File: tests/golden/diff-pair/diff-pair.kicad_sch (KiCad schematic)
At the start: 7 parts, among them J1 USB_MICRO_B, J2 CONN_BRK_1X04

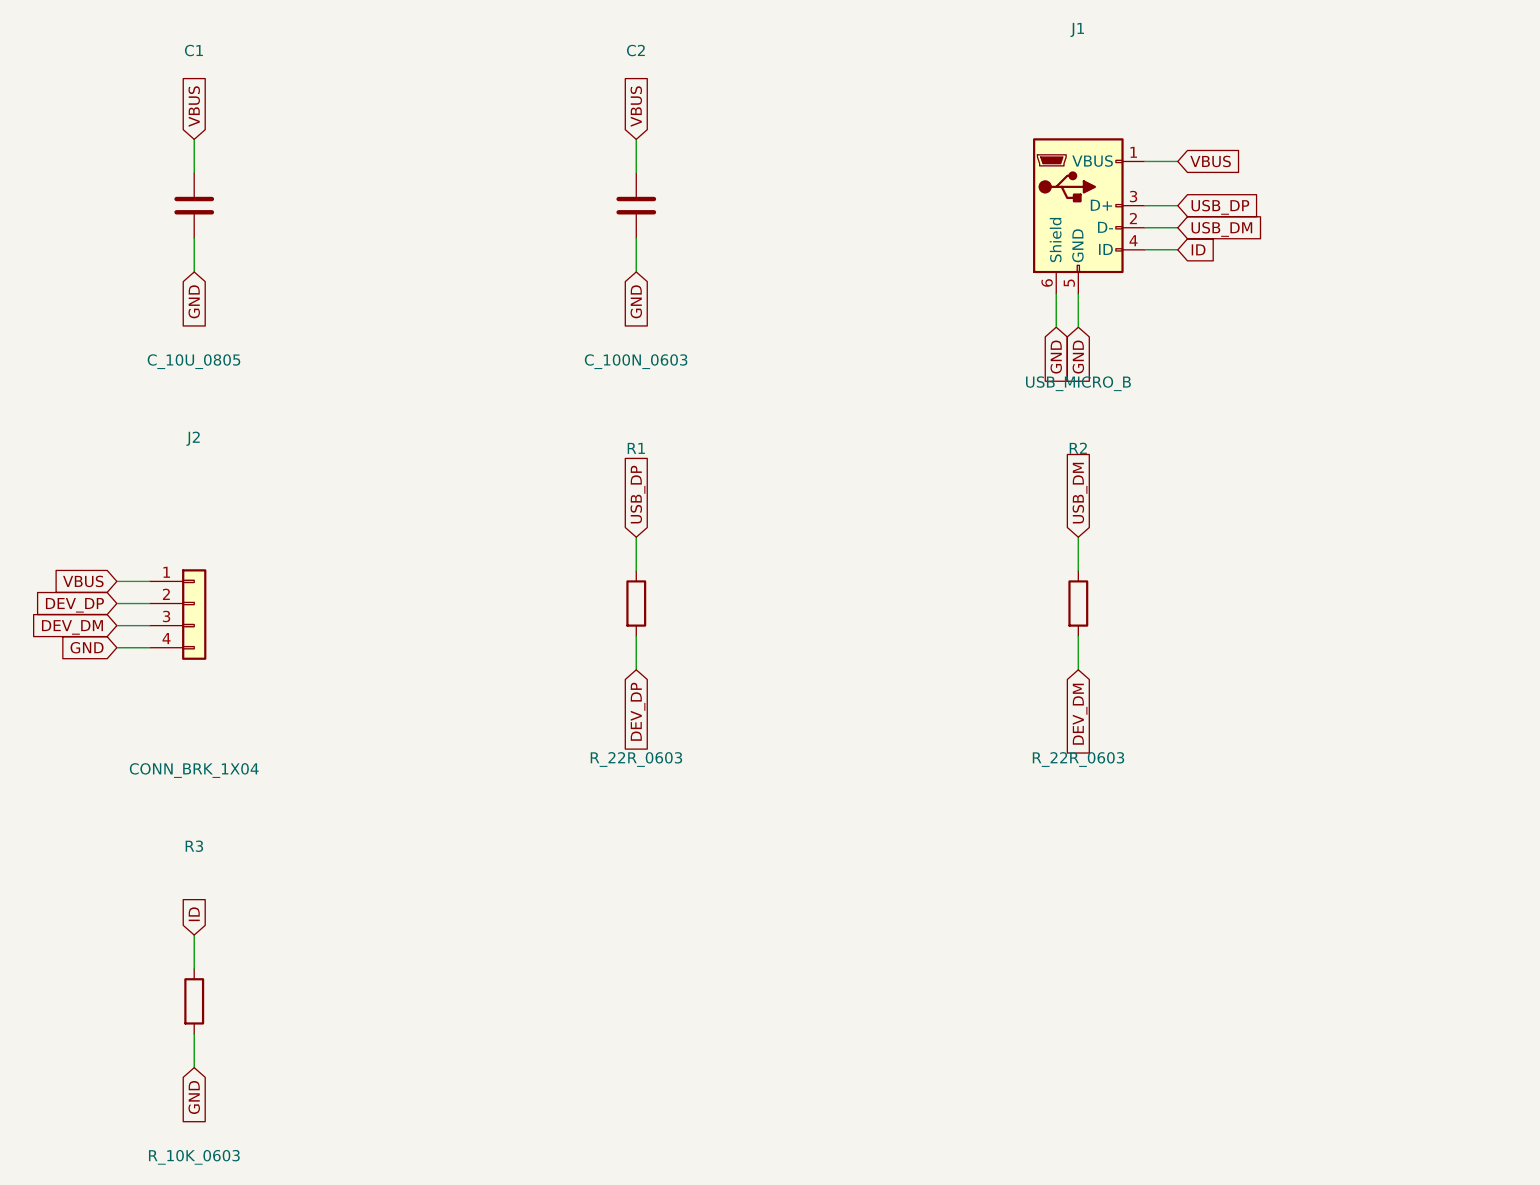
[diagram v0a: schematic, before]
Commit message: M7d: differential pairs routed as pairs, with honest limits
A pair's impedance comes from the coupling between its halves, so routing them
independently routes something else with the same netlist. A pair is now tightened
once, as a single centre-line wide enough for both traces and the gap, then offset
to either side. The gap is correct everywhere by construction, corners included,
and the halves come out the same length: 43.00 mm each with 0.000 mm skew on the
new diff-pair example.

Where a class gives an impedance but no gap, the gap is estimated from the standard
edge-coupled microstrip formula and reported as an estimate. Where the target is
unreachable by spacing at all — a 0.34 mm trace on 0.7 mm of dielectric spans only
about 102-195 ohm however far apart the halves go — that is said plainly rather
than clamped, because the fix is the trace width or the stackup and clamping would
hide it.

Coupled routing checks its own output and falls back rather than shipping something
that only looks like a pair. It refuses an ambiguous pair, one that would need a
crossover, one that would be mostly fan-out, and one whose fan-out would not clear
an obstacle it then names. Both of usb-port's pairs refuse, each saying which.

That self-checking is the reason DRC stays clean: the tightener guarantees
clearance for the centre-line, but the fan-out at each end is constructed rather
than tightened, and an early version of it landed 27 violations including shorts.
Checking beats hoping.

All five examples now route with zero DRC violations and zero schematic-parity
issues. Also implements `region_mm` placement rules, which the model promised and
the placer had been ignoring.

Not built, and said so in the docs rather than left to be discovered: meander
insertion for length matching, and pair crossovers. Skew is measured and reported
against the budget; nothing yet closes it.

Co-Authored-By: Claude Opus 5 (1M context) <noreply@anthropic.com>
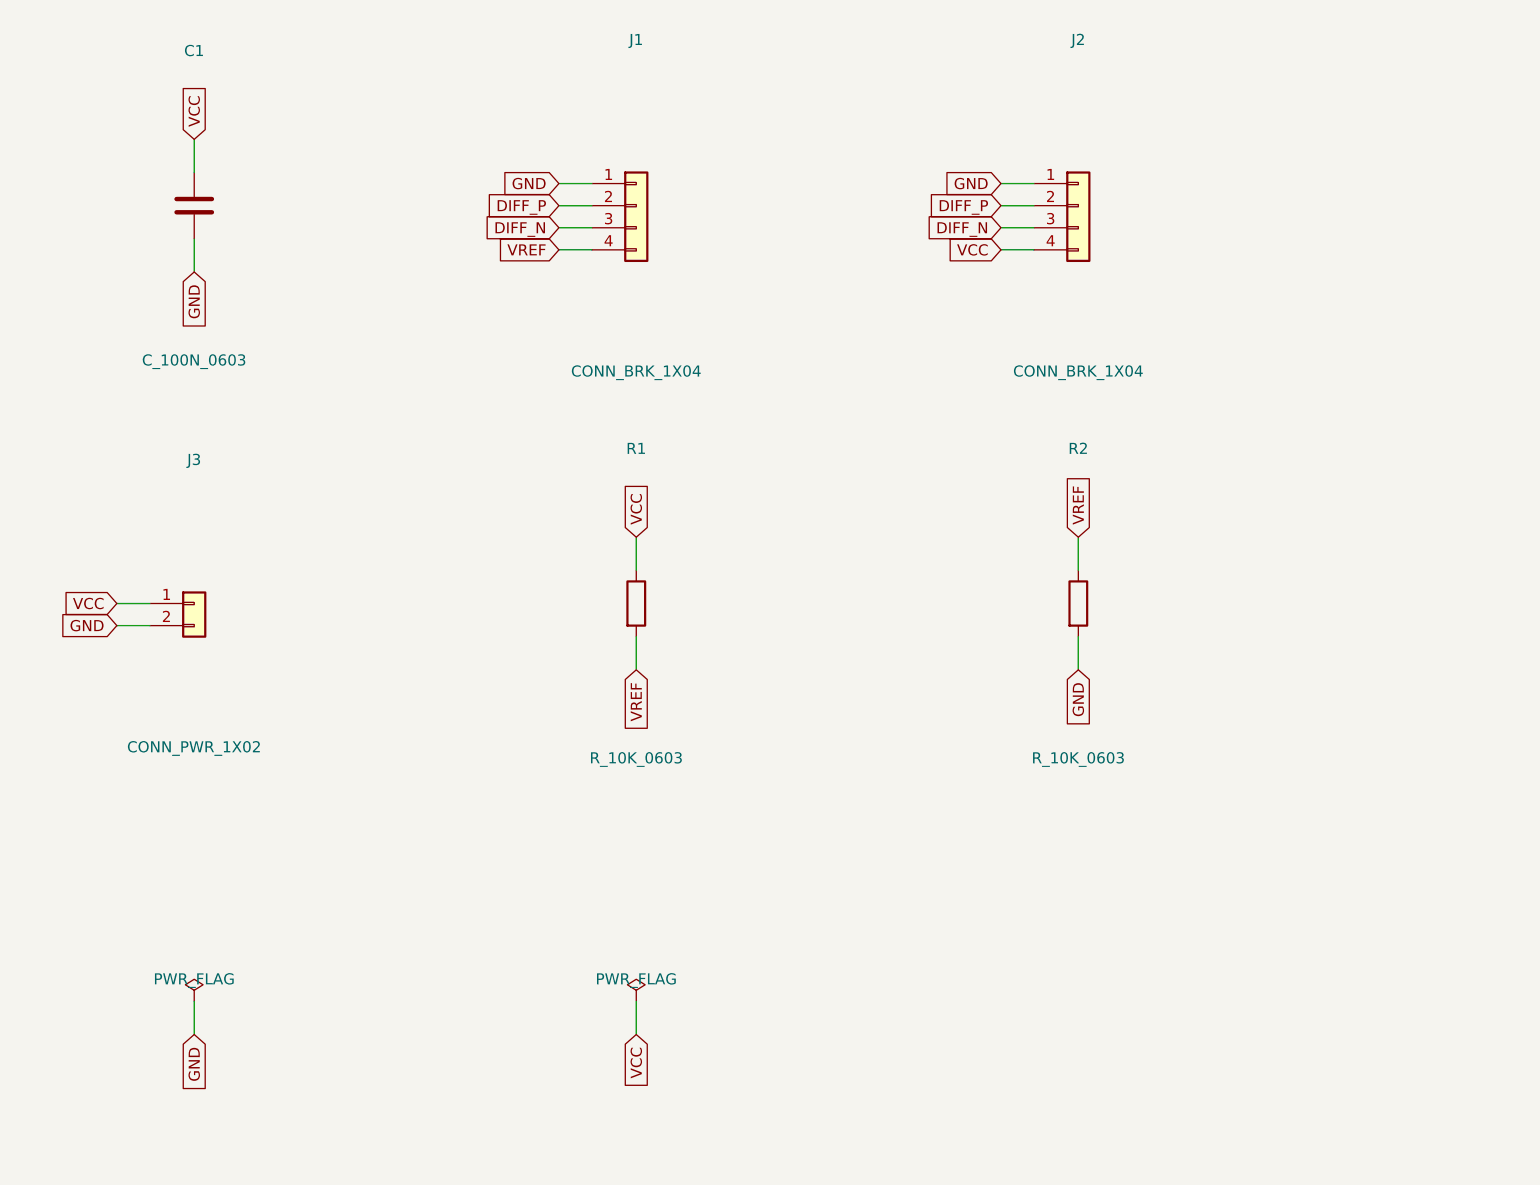
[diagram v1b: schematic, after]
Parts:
- removed C2: C_100N_0603, Capacitor_SMD:C_0603_1608Metric, symbol Device:C
- removed R3: R_10K_0603, Resistor_SMD:R_0603_1608Metric, symbol Device:R
- added J3: CONN_PWR_1X02, Connector_PinHeader_2.54mm:PinHeader_1x02_P2.54mm_Vertical, symbol Connector_Generic:Conn_01x02
- C1: value C_10U_0805 -> C_100N_0603; footprint Capacitor_SMD:C_0805_2012Metric -> Capacitor_SMD:C_0603_1608Metric; aipcb.reason Rides out the inrush when the cable is plugged in. -> (none); aipcb.role bulk -> decoupling
- J1: value USB_MICRO_B -> CONN_BRK_1X04; footprint Connector_USB:USB_Micro-B_Amphenol_10103594-0001LF_Horizontal -> Connector_PinHeader_2.54mm:PinHeader_1x04_P2.54mm_Vertical; symbol Connector:USB_B_Micro -> Connector_Generic:Conn_01x04; aipcb.reason Micro-B rather than Type-C, because this board is only ever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 -> Where the pair enters. Pins 2 and 3 carry it, adjacent, so 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
- J2: aipcb.reason Whatever consumes this port plugs in here. The pair is orde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 -> Where it leaves. The pair keeps the same order as at J1, so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
- R1: value R_22R_0603 -> R_10K_0603; aipcb.reason The 22 ohm series resistors set the driver's source impedan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 -> Upper leg of a reference divider. Deliberately *not* on the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; aipcb.role series -> divider
- R2: value R_22R_0603 -> R_10K_0603; aipcb.reason Partner of R1. Both must be the same value or the pair goes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 -> Lower leg. Same value, so the reference sits at half the ra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; aipcb.role series -> divider
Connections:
- net GND: now also J1.1 (Pin_1), J2.1 (Pin_1), R2.2, J3.2 (Pin_2); no longer J1.5 (GND), J1.6 (Shield), J2.4 (Pin_4)
- net DEV_DM renamed DIFF_N
- net DIFF_N: now also J1.3 (Pin_3); no longer R2.2
- net DEV_DP renamed DIFF_P
- net DIFF_P: now also J1.2 (Pin_2); no longer R1.2
- net ID renamed VREF
- net VREF: now also R1.2, R2.1
- removed net USB_DM: J1.2 (D-), R2.1
- net USB_DP renamed VCC
- net VCC: now also C1.1, J2.4 (Pin_4), J3.1 (Pin_1); no longer J1.3 (D+)
- removed net VBUS: C1.1, J1.1 (VBUS), J2.1 (Pin_1)
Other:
- title: usb-port -> diff-pair
- moved on the sheet: J2

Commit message: M14: the sheet that could not be reviewed, and the router that was never asked
Two themes. The generated schematics were electrically correct and unreadable:
every fact the source knew about *why* a part exists -- `role`, `for:`, the module
hierarchy, the netlist graph -- died at the sheet boundary, and a capacitor whose
purpose is to sit at one pin of one IC was placed by its position in a sorted list.
On pcie-sata that was 157.5 mm from the pin it decouples, on a sheet 594 mm wide.
And manual routing was something that *happened* to a board rather than something
the source could declare.

Placement is now derived in five steps (aipcb/compile/sheet.py): satellites attach
to what they serve, module instances become named clusters, blocks are ranked left
to right by breadth-first distance over signal nets only, ordered by a barycentre
sweep, and placed by measured extents. Rails point up, grounds point down, and a
crowded pin row keeps its labels because a ground symbol is wider than a 2.54 mm
pitch.

Measured across all eleven examples, before -> after:

  overlapping drawn items            71 -> 0
  mean decoupling-to-IC distance     down on every example with a local cap
    pcie-sata                     157.5 -> 27.8 mm
  total wire length                1196 -> 1151 mm
  wire crossings                      0 -> 0   (a stub idiom has none; said so)
  pcie-sata paper                    A1 -> A3

Nothing electrical moved, and it is proved rather than asserted: KiCad's own
netlister run against the pre- and post-M14 sheets agrees net name for net name and
pin for pin on all eleven; ERC is still 0; two builds are byte-identical; and
regenerating the golden tree moved eleven files, all of them .kicad_sch.

Three defects the *measurement* found, not the eye: KiCad's libraries stack a
part's repeated power pins on one coordinate and we drew nine identical GND labels
there; reference and value text was placed from the pin field rather than from the
drawing; and a block a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
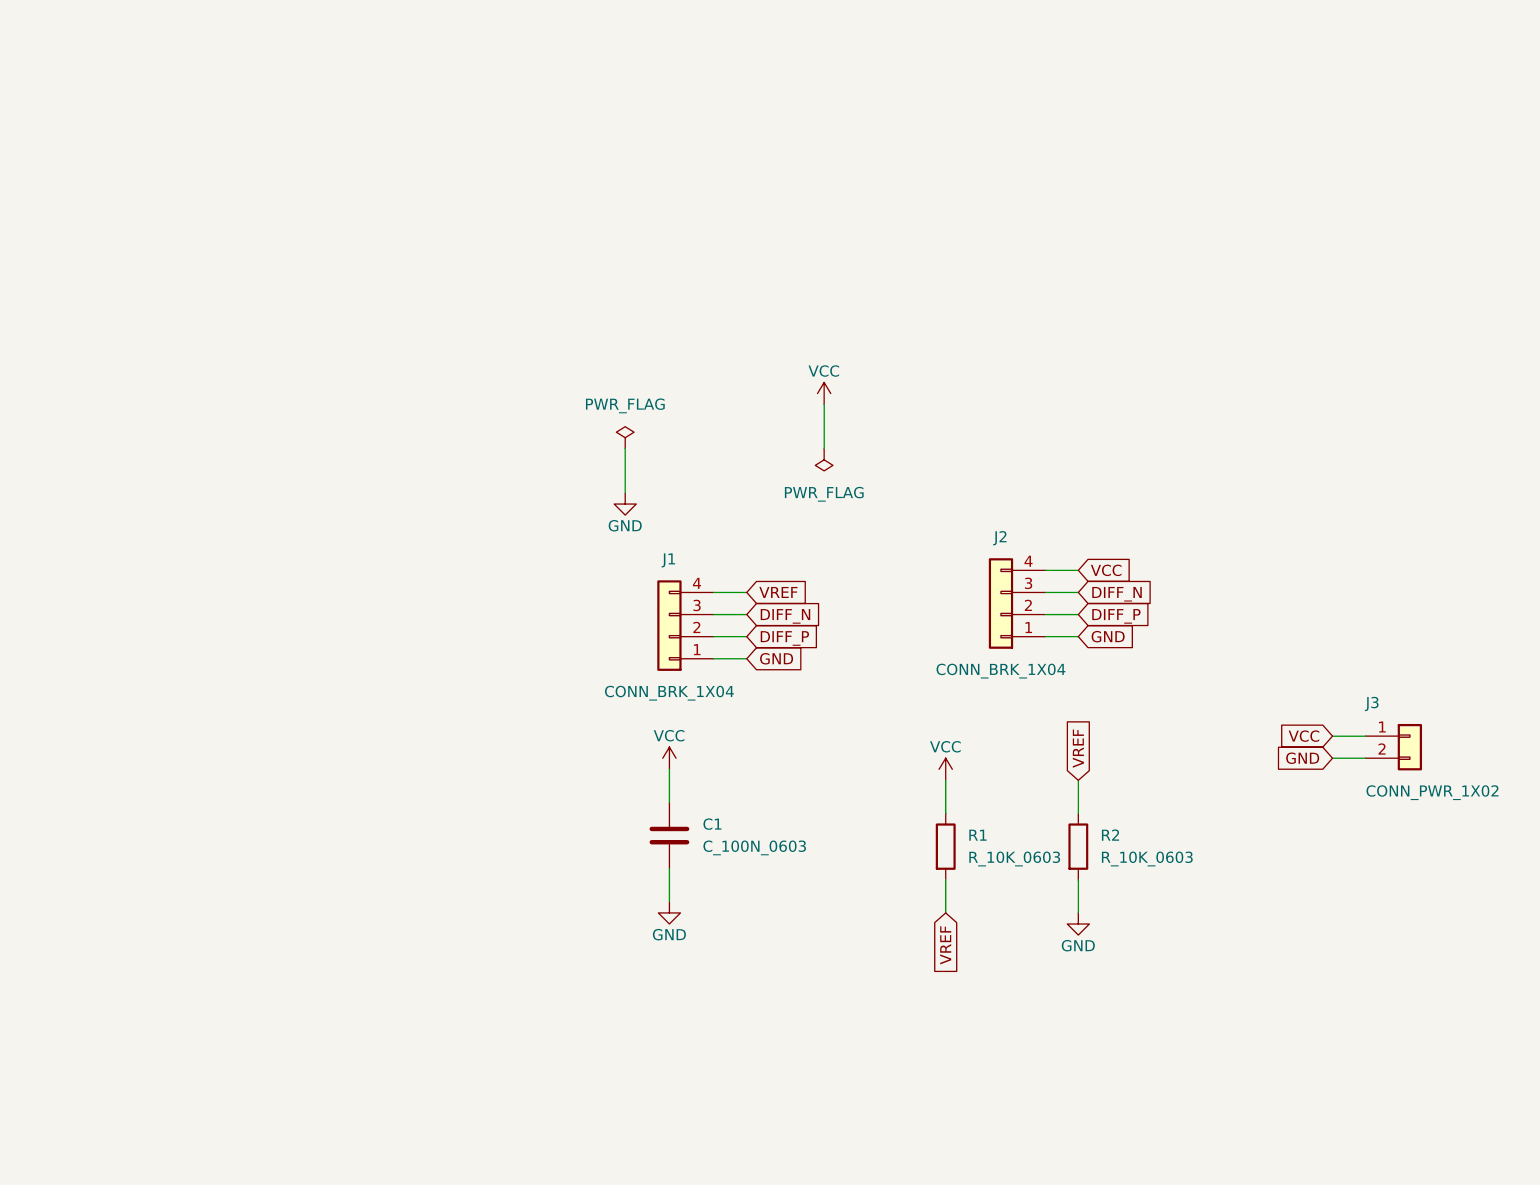
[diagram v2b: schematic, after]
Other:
- moved on the sheet: C1, J1, J2, J3, R1, R2
